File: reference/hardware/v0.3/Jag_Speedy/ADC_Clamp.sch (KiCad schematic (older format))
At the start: 1 part, among them IC10 SP720APP

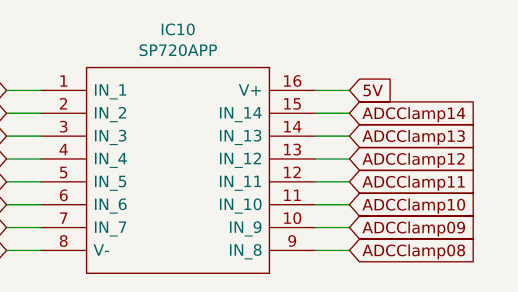
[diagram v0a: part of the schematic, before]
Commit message: Schematic pin mapping
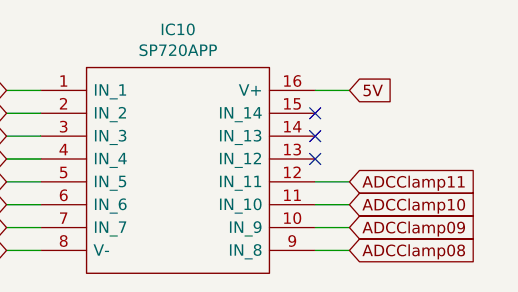
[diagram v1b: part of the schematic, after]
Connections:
- net ADCClamp12: no longer names the net of IC10.13 (IN_12)
- net ADCClamp13: no longer names the net of IC10.14 (IN_13)
- net ADCClamp14: no longer names the net of IC10.15 (IN_14)
- no-connect marks 0 -> 3
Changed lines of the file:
@@
 Text GLabel 4500 2000 0    50   Input ~ 0
 ADCClamp02
+Text GLabel 6000 1900 2    50   Input ~ 0
+5V
+Text GLabel 4500 2600 0    50   Input ~ 0
+SignalGnd
+Wire Wire Line
+	4500 1900 4650 1900
+Wire Wire Line
+	4650 2000 4500 2000
+Wire Wire Line
+	4650 2600 4500 2600
+Wire Wire Line
+	5850 1900 6000 1900
+NoConn ~ 5850 2000
+NoConn ~ 5850 2100
+NoConn ~ 5850 2200
 Text GLabel 4500 2100 0    50   Input ~ 0
 ADCClamp03
+Text GLabel 4500 2200 0    50   Input ~ 0
+ADCClamp04
 Text GLabel 4500 2300 0    50   Input ~ 0
 ADCClamp05
-Text GLabel 4500 2200 0    50   Input ~ 0
-ADCClamp04
 Text GLabel 4500 2400 0    50   Input ~ 0
 ADCClamp06
-Text GLabel 6000 1900 2    50   Input ~ 0
-5V
+Text GLabel 4500 2500 0    50   Input ~ 0
+ADCClamp07
+Text GLabel 6000 2600 2    50   Input ~ 0
+ADCClamp08
+Text GLabel 6000 2500 2    50   Input ~ 0
+ADCClamp09
+Text GLabel 6000 2400 2    50   Input ~ 0
+ADCClamp10
+Text GLabel 6000 2300 2    50   Input ~ 0
+ADCClamp11
 $Comp
 L SP720APP:SP720APP IC10
@@
 	1    0    0    -1
 $EndComp
-Text GLabel 4500 2600 0    50   Input ~ 0
-SignalGnd
-Text GLabel 4500 2500 0    50   Input ~ 0
-ADCClamp07
-Text GLabel 6000 2600 2    50   Input ~ 0
-ADCClamp08
-Text GLabel 6000 2500 2    50   Input ~ 0
-ADCClamp09
-Text GLabel 6000 2400 2    50   Input ~ 0
-ADCClamp10
-Text GLabel 6000 2300 2    50   Input ~ 0
-ADCClamp11
-Text GLabel 6000 2200 2    50   Input ~ 0
-ADCClamp12
-Text GLabel 6000 2100 2    50   Input ~ 0
-ADCClamp13
-Text GLabel 6000 2000 2    50   Input ~ 0
-ADCClamp14
-Wire Wire Line
-	4500 1900 4650 1900
-Wire Wire Line
-	4650 2000 4500 2000
 Wire Wire Line
 	4500 2100 4650 2100
@@
 	4500 2500 4650 2500
 Wire Wire Line
-	4650 2600 4500 2600
+	5850 2600 6000 2600
 Wire Wire Line
-	5850 1900 6000 1900
+	6000 2500 5850 2500
 Wire Wire Line
-	6000 2000 5850 2000
+	5850 2400 6000 2400
 Wire Wire Line
-	5850 2100 6000 2100
-Wire Wire Line
-	6000 2200 5850 2200
-Wire Wire Line
-	5850 2300 6000 2300
-Wire Wire Line
-	6000 2400 5850 2400
-Wire Wire Line
-	5850 2500 6000 2500
-Wire Wire Line
-	6000 2600 5850 2600
+	6000 2300 5850 2300
 $EndSCHEMATC

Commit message: MOSFET Drivers
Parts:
- IC10: symbol SP720APP:SP720APP -> Jag_Speedy-rescue:SP720APP-SP720APP
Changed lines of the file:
@@
 ADCClamp11
 $Comp
-L SP720APP:SP720APP IC10
+L Jag_Speedy-rescue:SP720APP-SP720APP IC10
 U 1 1 5F118B50
 P 4650 1900

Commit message: Rationalise level shifting
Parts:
- added IC12: SP720APP, Package_DIP:DIP-16_W7.62mm, symbol Jag_Speedy-rescue:SP720APP-SP720APP-Jag_Speedy-rescue
- added R1, R2, R7, R8: 180k, Resistor_THT:R_Axial_DIN0207_L6.3mm_D2.5mm_P2.54mm_Vertical, symbol Device:R
- added R3, R4, R5, R6: 330k, Resistor_THT:R_Axial_DIN0207_L6.3mm_D2.5mm_P2.54mm_Vertical, symbol Device:R
- added U1: LMV324, Package_DIP:DIP-14_W7.62mm_Socket, symbol Amplifier_Operational:LMV324
- IC10: symbol Jag_Speedy-rescue:SP720APP-SP720APP -> Jag_Speedy-rescue:SP720APP-SP720APP-Jag_Speedy-rescue
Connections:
- net ADCClamp05: now also IC12.1 (IN_1); no longer IC10.5 (IN_5)
- net ADCClamp09: now also IC12.9 (IN_8); no longer IC10.10 (IN_9)
- net ADCClamp10: now also IC12.10 (IN_9); no longer IC10.11 (IN_10)
- net ADCClamp11: now also IC12.11 (IN_10); no longer IC10.12 (IN_11)
- net SignalGnd: now also IC12.8 (V-), R3.2, R4.2, R5.1, R6.1, U1.11 (V-)
- new net: R1.2, R4.1, U1.12 (+)
- new net: R6.2, R8.1, U1.10 (+)
- new net: R2.2, R3.1, U1.5 (+)
- new net: R5.2, R7.1, U1.3 (+)
- new net 3V3: IC12.16 (V+), U1.4 (V+)
- new net Barro-Signal-3.3V: U1.6 (-), U1.7
- new net Barro-Signal-5V: R2.1
- new net MAP-Signal-3.3V: U1.13 (-), U1.14
- new net MAP-Signal-5V: R1.1
- new net O2-Signal-3.3V: U1.1, U1.2 (-)
- new net O2-Signal-5V: R7.2
- new net TPS-Signal-3.3V: U1.8, U1.9 (-)
- new net TPS-Signal-5V: R8.2
- no-connect marks 3 -> 17
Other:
- moved on the sheet: IC10

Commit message: SMD Update
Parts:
- IC10, IC12: footprint Package_DIP:DIP-16_W7.62mm -> Package_SO:SOIC-16_3.9x9.9mm_P1.27mm
- R1, R2, R3, R4, R5, R6, R7, R8: footprint Resistor_THT:R_Axial_DIN0207_L6.3mm_D2.5mm_P2.54mm_Vertical -> Resistor_SMD:R_0805_2012Metric
- U1: footprint Package_DIP:DIP-14_W7.62mm_Socket -> Package_SO:SO-14_5.3x10.2mm_P1.27mm
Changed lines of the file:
@@
 F 0 "IC10" H 2600 1815 50  0000 C CNN
 F 1 "SP720APP" H 2600 1724 50  0000 C CNN
-F 2 "Package_DIP:DIP-16_W7.62mm" H 3050 1650 50  0001 L CNN
+F 2 "Package_SO:SOIC-16_3.9x9.9mm_P1.27mm" H 3050 1650 50  0001 L CNN
 F 3 "https://componentsearchengine.com/Datasheets/1/SP720APP.pdf" H 3050 1550 50  0001 L CNN
 F 4 "TVS Diode Arrays 14 CH DIODE ARRAY" H 3050 1450 50  0001 L CNN "Description"
@@
 F 0 "IC12" H 2600 3115 50  0000 C CNN
 F 1 "SP720APP" H 2600 3024 50  0000 C CNN
-F 2 "Package_DIP:DIP-16_W7.62mm" H 3050 2950 50  0001 L CNN
+F 2 "Package_SO:SOIC-16_3.9x9.9mm_P1.27mm" H 3050 2950 50  0001 L CNN
 F 3 "https://componentsearchengine.com/Datasheets/1/SP720APP.pdf" H 3050 2850 50  0001 L CNN
 F 4 "TVS Diode Arrays 14 CH DIODE ARRAY" H 3050 2750 50  0001 L CNN "Description"
@@
 F 0 "U1" V 6945 3600 50  0000 C CNN
 F 1 "LMV324" V 6854 3600 50  0000 C CNN
-F 2 "Package_DIP:DIP-14_W7.62mm_Socket" H 6800 3700 50  0001 C CNN
+F 2 "Package_SO:SO-14_5.3x10.2mm_P1.27mm" H 6800 3700 50  0001 C CNN
 F 3 "http://www.ti.com/lit/ds/symlink/lmv324.pdf" H 6900 3800 50  0001 C CNN
 	5    6850 3600
@@
 F 0 "U1" V 6354 3180 50  0000 L CNN
 F 1 "LMV324" V 6445 3180 50  0000 L CNN
-F 2 "Package_DIP:DIP-14_W7.62mm_Socket" H 6350 3050 50  0001 C CNN
+F 2 "Package_SO:SO-14_5.3x10.2mm_P1.27mm" H 6350 3050 50  0001 C CNN
 F 3 "http://www.ti.com/lit/ds/symlink/lmv324.pdf" H 6450 3150 50  0001 C CNN
 	4    6400 2950
@@
 F 0 "U1" V 7154 3180 50  0000 L CNN
 F 1 "LMV324" V 7245 3180 50  0000 L CNN
-F 2 "Package_DIP:DIP-14_W7.62mm_Socket" H 7150 3050 50  0001 C CNN
+F 2 "Package_SO:SO-14_5.3x10.2mm_P1.27mm" H 7150 3050 50  0001 C CNN
 F 3 "http://www.ti.com/lit/ds/symlink/lmv324.pdf" H 7250 3150 50  0001 C CNN
 	3    7200 2950
@@
 F 0 "U1" V 6354 2080 50  0000 L CNN
 F 1 "LMV324" V 6445 2080 50  0000 L CNN
-F 2 "Package_DIP:DIP-14_W7.62mm_Socket" H 6350 1950 50  0001 C CNN
+F 2 "Package_SO:SO-14_5.3x10.2mm_P1.27mm" H 6350 1950 50  0001 C CNN
 F 3 "http://www.ti.com/lit/ds/symlink/lmv324.pdf" H 6450 2050 50  0001 C CNN
 	2    6400 1850
@@
 F 0 "U1" V 7154 2080 50  0000 L CNN
 F 1 "LMV324" V 7245 2080 50  0000 L CNN
-F 2 "Package_DIP:DIP-14_W7.62mm_Socket" H 7150 1950 50  0001 C CNN
+F 2 "Package_SO:SO-14_5.3x10.2mm_P1.27mm" H 7150 1950 50  0001 C CNN
 F 3 "http://www.ti.com/lit/ds/symlink/lmv324.pdf" H 7250 2050 50  0001 C CNN
 	1    7200 1850
@@
 F 0 "R8" V 7707 2550 50  0000 C CNN
 F 1 "180k" V 7616 2550 50  0000 C CNN
-F 2 "Resistor_THT:R_Axial_DIN0207_L6.3mm_D2.5mm_P2.54mm_Vertical" V 7430 2550 50  0001 C CNN
+F 2 "Resistor_SMD:R_0805_2012Metric" V 7430 2550 50  0001 C CNN
 F 3 "~" H 7500 2550 50  0001 C CNN
 	1    7500 2550
@@
 F 0 "R6" V 7307 2550 50  0000 C CNN
 F 1 "330k" V 7216 2550 50  0000 C CNN
-F 2 "Resistor_THT:R_Axial_DIN0207_L6.3mm_D2.5mm_P2.54mm_Vertical" V 7030 2550 50  0001 C CNN
+F 2 "Resistor_SMD:R_0805_2012Metric" V 7030 2550 50  0001 C CNN
 F 3 "~" H 7100 2550 50  0001 C CNN
 	1    7100 2550
@@
 F 0 "R4" V 6907 2550 50  0000 C CNN
 F 1 "330k" V 6816 2550 50  0000 C CNN
-F 2 "Resistor_THT:R_Axial_DIN0207_L6.3mm_D2.5mm_P2.54mm_Vertical" V 6630 2550 50  0001 C CNN
+F 2 "Resistor_SMD:R_0805_2012Metric" V 6630 2550 50  0001 C CNN
 F 3 "~" H 6700 2550 50  0001 C CNN
 	1    6700 2550
@@
 F 0 "R1" V 6407 2550 50  0000 C CNN
 F 1 "180k" V 6316 2550 50  0000 C CNN
-F 2 "Resistor_THT:R_Axial_DIN0207_L6.3mm_D2.5mm_P2.54mm_Vertical" V 6130 2550 50  0001 C CNN
+F 2 "Resistor_SMD:R_0805_2012Metric" V 6130 2550 50  0001 C CNN
 F 3 "~" H 6200 2550 50  0001 C CNN
 	1    6200 2550
@@
 F 0 "R3" V 6907 1450 50  0000 C CNN
 F 1 "330k" V 6816 1450 50  0000 C CNN
-F 2 "Resistor_THT:R_Axial_DIN0207_L6.3mm_D2.5mm_P2.54mm_Vertical" V 6630 1450 50  0001 C CNN
+F 2 "Resistor_SMD:R_0805_2012Metric" V 6630 1450 50  0001 C CNN
 F 3 "~" H 6700 1450 50  0001 C CNN
 	1    6700 1450
@@
 F 0 "R2" V 6457 1450 50  0000 C CNN
 F 1 "180k" V 6366 1450 50  0000 C CNN
-F 2 "Resistor_THT:R_Axial_DIN0207_L6.3mm_D2.5mm_P2.54mm_Vertical" V 6180 1450 50  0001 C CNN
+F 2 "Resistor_SMD:R_0805_2012Metric" V 6180 1450 50  0001 C CNN
 F 3 "~" H 6250 1450 50  0001 C CNN
 	1    6250 1450
@@
 F 0 "R7" V 7707 1450 50  0000 C CNN
 F 1 "180k" V 7616 1450 50  0000 C CNN
-F 2 "Resistor_THT:R_Axial_DIN0207_L6.3mm_D2.5mm_P2.54mm_Vertical" V 7430 1450 50  0001 C CNN
+F 2 "Resistor_SMD:R_0805_2012Metric" V 7430 1450 50  0001 C CNN
 F 3 "~" H 7500 1450 50  0001 C CNN
 	1    7500 1450
@@
 F 0 "R5" V 7307 1450 50  0000 C CNN
 F 1 "330k" V 7216 1450 50  0000 C CNN
-F 2 "Resistor_THT:R_Axial_DIN0207_L6.3mm_D2.5mm_P2.54mm_Vertical" V 7030 1450 50  0001 C CNN
+F 2 "Resistor_SMD:R_0805_2012Metric" V 7030 1450 50  0001 C CNN
 F 3 "~" H 7100 1450 50  0001 C CNN
 	1    7100 1450

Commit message: VR Conditioner
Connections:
- net ADCClamp08: now also IC10.5 (IN_5); no longer IC10.9 (IN_8)
- net ADCClamp10: now also IC12.3 (IN_3); no longer IC12.10 (IN_9)
- net ADCClamp11: now also IC12.2 (IN_2); no longer IC12.11 (IN_10)
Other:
- note added: "ADC Clamping"
- note added: "Level Shifting"
- moved on the sheet: R1, R4, R6, R8, U1C, U1D, U1E
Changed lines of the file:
@@
 Text GLabel 1850 2150 0    50   Input ~ 0
 ADCClamp07
-Text GLabel 3350 2250 2    50   Input ~ 0
+Text GLabel 1850 1950 0    50   Input ~ 0
 ADCClamp08
 Text GLabel 3350 3550 2    50   Input ~ 0
 ADCClamp09
-Text GLabel 3350 3450 2    50   Input ~ 0
+Text GLabel 1850 3050 0    50   Input ~ 0
 ADCClamp10
-Text GLabel 3350 3350 2    50   Input ~ 0
+Text GLabel 1850 2950 0    50   Input ~ 0
 ADCClamp11
 $Comp
@@
 Text GLabel 3350 2850 2    50   Input ~ 0
 3V3
-NoConn ~ 1850 1950
 Wire Wire Line
 	3350 2850 3200 2850
@@
 NoConn ~ 3350 2150
 NoConn ~ 3350 2050
-Wire Wire Line
-	3350 3450 3200 3450
-Wire Wire Line
-	3350 3350 3200 3350
 NoConn ~ 3350 1950
 $Comp
 L Amplifier_Operational:LMV324 U?
 U 5 1 5F0A9466
-P 6850 3600
+P 6900 3900
 AR Path="/5F0A9466" Ref="U?"  Part="5"
 AR Path="/5EF0F56B/5F0A9466" Ref="U1"  Part="5"
-F 0 "U1" V 6945 3600 50  0000 C CNN
-F 1 "LMV324" V 6854 3600 50  0000 C CNN
-F 2 "Package_SO:SO-14_5.3x10.2mm_P1.27mm" H 6800 3700 50  0001 C CNN
-F 3 "http://www.ti.com/lit/ds/symlink/lmv324.pdf" H 6900 3800 50  0001 C CNN
-	5    6850 3600
+F 0 "U1" V 6995 3900 50  0000 C CNN
+F 1 "LMV324" V 6904 3900 50  0000 C CNN
+F 2 "Package_SO:SO-14_5.3x10.2mm_P1.27mm" H 6850 4000 50  0001 C CNN
+F 3 "http://www.ti.com/lit/ds/symlink/lmv324.pdf" H 6950 4100 50  0001 C CNN
+	5    6900 3900
 	0    -1   -1   0
 $EndComp
@@
 L Amplifier_Operational:LMV324 U?
 U 4 1 5F0A946C
-P 6400 2950
+P 6450 3250
 AR Path="/5F0A946C" Ref="U?"  Part="4"
 AR Path="/5EF0F56B/5F0A946C" Ref="U1"  Part="4"
-F 0 "U1" V 6354 3180 50  0000 L CNN
-F 1 "LMV324" V 6445 3180 50  0000 L CNN
-F 2 "Package_SO:SO-14_5.3x10.2mm_P1.27mm" H 6350 3050 50  0001 C CNN
-F 3 "http://www.ti.com/lit/ds/symlink/lmv324.pdf" H 6450 3150 50  0001 C CNN
-	4    6400 2950
+F 0 "U1" V 6404 3480 50  0000 L CNN
+F 1 "LMV324" V 6495 3480 50  0000 L CNN
+F 2 "Package_SO:SO-14_5.3x10.2mm_P1.27mm" H 6400 3350 50  0001 C CNN
+F 3 "http://www.ti.com/lit/ds/symlink/lmv324.pdf" H 6500 3450 50  0001 C CNN
+	4    6450 3250
 	0    1    1    0
 $EndComp
@@
 L Amplifier_Operational:LMV324 U?
 U 3 1 5F0A9472
-P 7200 2950
+P 7250 3250
 AR Path="/5F0A9472" Ref="U?"  Part="3"
 AR Path="/5EF0F56B/5F0A9472" Ref="U1"  Part="3"
-F 0 "U1" V 7154 3180 50  0000 L CNN
-F 1 "LMV324" V 7245 3180 50  0000 L CNN
-F 2 "Package_SO:SO-14_5.3x10.2mm_P1.27mm" H 7150 3050 50  0001 C CNN
-F 3 "http://www.ti.com/lit/ds/symlink/lmv324.pdf" H 7250 3150 50  0001 C CNN
-	3    7200 2950
+F 0 "U1" V 7204 3480 50  0000 L CNN
+F 1 "LMV324" V 7295 3480 50  0000 L CNN
+F 2 "Package_SO:SO-14_5.3x10.2mm_P1.27mm" H 7200 3350 50  0001 C CNN
+F 3 "http://www.ti.com/lit/ds/symlink/lmv324.pdf" H 7300 3450 50  0001 C CNN
+	3    7250 3250
 	0    1    1    0
 $EndComp
@@
 Text GLabel 7750 1450 2    50   Input ~ 0
 O2-Signal-5V
-Text GLabel 7750 3250 2    50   Output ~ 0
+Text GLabel 7800 3550 2    50   Output ~ 0
 TPS-Signal-3.3V
 $Comp
 L Device:R R?
 U 1 1 5F0A9487
-P 7500 2550
+P 7550 2850
 AR Path="/5F0A9487" Ref="R?"  Part="1"
 AR Path="/5EF0F56B/5F0A9487" Ref="R8"  Part="1"
-F 0 "R8" V 7707 2550 50  0000 C CNN
-F 1 "180k" V 7616 2550 50  0000 C CNN
-F 2 "Resistor_SMD:R_0805_2012Metric" V 7430 2550 50  0001 C CNN
-F 3 "~" H 7500 2550 50  0001 C CNN
-	1    7500 2550
+F 0 "R8" V 7757 2850 50  0000 C CNN
+F 1 "180k" V 7666 2850 50  0000 C CNN
+F 2 "Resistor_SMD:R_0805_2012Metric" V 7480 2850 50  0001 C CNN
+F 3 "~" H 7550 2850 50  0001 C CNN
+	1    7550 2850
 	0    -1   -1   0
 $EndComp
@@
 L Device:R R?
 U 1 1 5F0A948D
-P 7100 2550
+P 7150 2850
 AR Path="/5F0A948D" Ref="R?"  Part="1"
 AR Path="/5EF0F56B/5F0A948D" Ref="R6"  Part="1"
-F 0 "R6" V 7307 2550 50  0000 C CNN
-F 1 "330k" V 7216 2550 50  0000 C CNN
-F 2 "Resistor_SMD:R_0805_2012Metric" V 7030 2550 50  0001 C CNN
-F 3 "~" H 7100 2550 50  0001 C CNN
-	1    7100 2550
+F 0 "R6" V 7357 2850 50  0000 C CNN
+F 1 "330k" V 7266 2850 50  0000 C CNN
+F 2 "Resistor_SMD:R_0805_2012Metric" V 7080 2850 50  0001 C CNN
+F 3 "~" H 7150 2850 50  0001 C CNN
+	1    7150 2850
 	0    -1   -1   0
 $EndComp
@@
 L Device:R R?
 U 1 1 5F0A9493
-P 6700 2550
+P 6750 2850
 AR Path="/5F0A9493" Ref="R?"  Part="1"
 AR Path="/5EF0F56B/5F0A9493" Ref="R4"  Part="1"
-F 0 "R4" V 6907 2550 50  0000 C CNN
-F 1 "330k" V 6816 2550 50  0000 C CNN
-F 2 "Resistor_SMD:R_0805_2012Metric" V 6630 2550 50  0001 C CNN
-F 3 "~" H 6700 2550 50  0001 C CNN
-	1    6700 2550
+F 0 "R4" V 6957 2850 50  0000 C CNN
+F 1 "330k" V 6866 2850 50  0000 C CNN
+F 2 "Resistor_SMD:R_0805_2012Metric" V 6680 2850 50  0001 C CNN
+F 3 "~" H 6750 2850 50  0001 C CNN
+	1    6750 2850
 	0    -1   -1   0
 $EndComp
@@
 L Device:R R?
 U 1 1 5F0A9499
-P 6200 2550
+P 6250 2850
 AR Path="/5F0A9499" Ref="R?"  Part="1"
 AR Path="/5EF0F56B/5F0A9499" Ref="R1"  Part="1"
-F 0 "R1" V 6407 2550 50  0000 C CNN
-F 1 "180k" V 6316 2550 50  0000 C CNN
-F 2 "Resistor_SMD:R_0805_2012Metric" V 6130 2550 50  0001 C CNN
-F 3 "~" H 6200 2550 50  0001 C CNN
-	1    6200 2550
-	0    -1   -1   0
-$EndComp
-Text GLabel 5950 2550 0    50   Input ~ 0
+F 0 "R1" V 6457 2850 50  0000 C CNN
+F 1 "180k" V 6366 2850 50  0000 C CNN
+F 2 "Resistor_SMD:R_0805_2012Metric" V 6180 2850 50  0001 C CNN
+F 3 "~" H 6250 2850 50  0001 C CNN
+	1    6250 2850
+	0    -1   -1   0
+$EndComp
+Text GLabel 6000 2850 0    50   Input ~ 0
 MAP-Signal-5V
 Wire Wire Line
-	5950 2550 6050 2550
-Wire Wire Line
-	6350 2550 6500 2550
-Wire Wire Line
-	7250 2550 7300 2550
-Wire Wire Line
-	7300 2650 7300 2550
-Connection ~ 7300 2550
-Wire Wire Line
-	7300 2550 7350 2550
-Wire Wire Line
-	6500 2650 6500 2550
-Connection ~ 6500 2550
-Wire Wire Line
-	6500 2550 6550 2550
-Text GLabel 6500 3700 0    50   Input ~ 0
+	6000 2850 6100 2850
+Wire Wire Line
+	6400 2850 6550 2850
+Wire Wire Line
+	7300 2850 7350 2850
+Wire Wire Line
+	7350 2950 7350 2850
+Connection ~ 7350 2850
+Wire Wire Line
+	7350 2850 7400 2850
+Wire Wire Line
+	6550 2950 6550 2850
+Connection ~ 6550 2850
+Wire Wire Line
+	6550 2850 6600 2850
+Text GLabel 6550 4000 0    50   Input ~ 0
 3V3
 Wire Wire Line
-	6500 3700 6550 3700
-Wire Wire Line
-	6400 3350 6400 3250
-Wire Wire Line
-	7100 2650 6950 2650
-Wire Wire Line
-	6950 2650 6950 3250
-Wire Wire Line
-	6950 3250 7200 3250
-Wire Wire Line
-	6300 2650 6150 2650
-Wire Wire Line
-	6150 2650 6150 3350
-Wire Wire Line
-	6150 3350 6400 3350
-Connection ~ 6400 3350
-Wire Wire Line
-	7750 3250 7200 3250
-Connection ~ 7200 3250
-Wire Wire Line
-	6400 3350 7750 3350
-Text GLabel 5950 1450 0    50   Input ~ 0
+	6550 4000 6600 4000
+Wire Wire Line
+	6450 3650 6450 3550
+Wire Wire Line
+	7150 2950 7000 2950
+Wire Wire Line
+	7000 2950 7000 3550
+Wire Wire Line
+	7000 3550 7250 3550
+Wire Wire Line
+	6350 2950 6200 2950
+Wire Wire Line
+	6200 2950 6200 3650
+Wire Wire Line
+	6200 3650 6450 3650
+Connection ~ 6450 3650
+Wire Wire Line
+	7800 3550 7250 3550
+Connection ~ 7250 3550
+Wire Wire Line
+	6450 3650 7800 3650
+Text GLabel 6000 1450 0    50   Input ~ 0
 Barro-Signal-5V
 Wire Wire Line
-	7650 2550 7750 2550
-Text GLabel 7750 2550 2    50   Input ~ 0
+	7700 2850 7800 2850
+Text GLabel 7800 2850 2    50   Input ~ 0
 TPS-Signal-5V
 Text GLabel 7800 2250 2    50   Output ~ 0
@@
 $EndComp
 Wire Wire Line
-	5950 1450 6100 1450
-Wire Wire Line
 	6400 1450 6500 1450
 Wire Wire Line
@@
 Wire Wire Line
 	7750 1450 7650 1450
-Text GLabel 7250 3700 2    50   Input ~ 0
+Text GLabel 7300 4000 2    50   Input ~ 0
 SignalGnd
 Wire Wire Line
-	7250 3700 7150 3700
-Wire Wire Line
-	6850 2550 6950 2550
-Text GLabel 6900 2550 3    50   Input ~ 0
+	7300 4000 7200 4000
+Wire Wire Line
+	6900 2850 6950 2850
+Text GLabel 6950 2750 1    50   Input ~ 0
 SignalGnd
-Text GLabel 6900 1450 3    50   Input ~ 0
+Text GLabel 6900 1350 1    50   Input ~ 0
 SignalGnd
-Text GLabel 7750 3350 2    50   Output ~ 0
+Text GLabel 7800 3650 2    50   Output ~ 0
 MAP-Signal-3.3V
 Wire Wire Line
@@
 	6400 2250 7800 2250
 Wire Wire Line
-	6850 1450 6950 1450
-NoConn ~ 2000 2950
-NoConn ~ 2000 3050
+	6850 1450 6900 1450
 NoConn ~ 2000 3150
 NoConn ~ 2000 3250
@@
 Wire Wire Line
 	1800 3550 2000 3550
+Wire Wire Line
+	2000 2950 1850 2950
+Wire Wire Line
+	1850 3050 2000 3050
+NoConn ~ 3200 3450
+NoConn ~ 3200 3350
+NoConn ~ 3350 2250
+Wire Wire Line
+	6900 1350 6900 1450
+Connection ~ 6900 1450
+Wire Wire Line
+	6900 1450 6950 1450
+Wire Wire Line
+	6950 2750 6950 2850
+Connection ~ 6950 2850
+Wire Wire Line
+	6950 2850 7000 2850
+Wire Wire Line
+	6000 1450 6100 1450
+Text Notes 1650 1050 0    157  ~ 0
+ADC Clamping
+Text Notes 6300 850  0    157  ~ 0
+Level Shifting
 $EndSCHEMATC
